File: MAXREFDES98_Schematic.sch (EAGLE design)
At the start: 17 parts, among them T1 TG110-S055N2RL

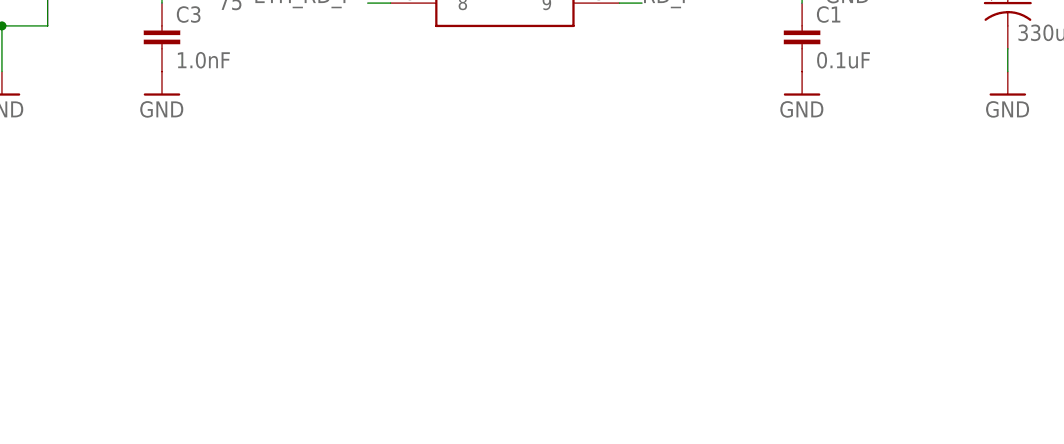
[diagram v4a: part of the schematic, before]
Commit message: Added ethernet jumpers
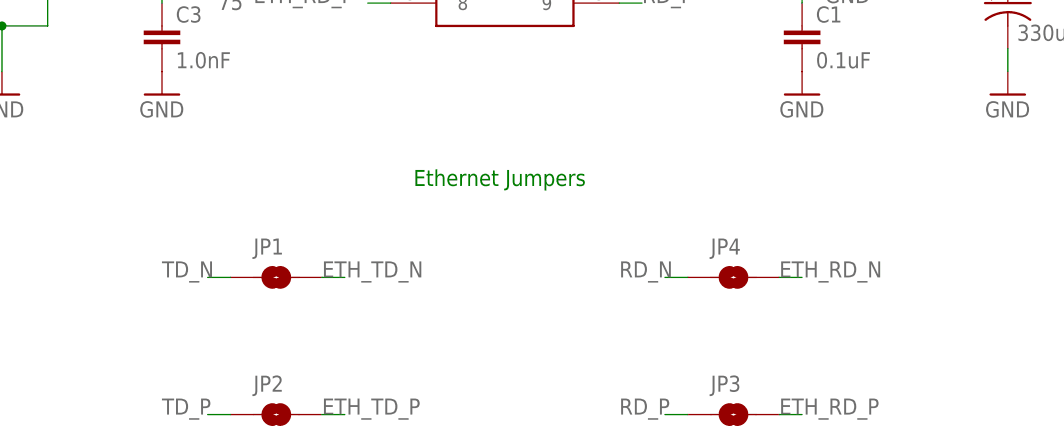
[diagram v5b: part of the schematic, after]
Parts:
- added JP1, JP2, JP3, JP4: JUMPER-SMT_2_NO_NO-SILK, SparkFun-Jumpers:JUMPER-SMT_2_NO_NO-SILK
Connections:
- net ETH_RD_N: now also JP4.2
- net ETH_RD_P: now also JP3.2
- net ETH_TD_N: now also JP1.2
- net ETH_TD_P: now also JP2.2
- net RD_N: now also JP4.1
- net RD_P: now also JP3.1
- net TD_N: now also JP1.1
- net TD_P: now also JP2.1
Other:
- note added: "Ethernet Jumpers"
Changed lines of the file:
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@@
 <part name="GND8" library="supply1" library_urn="urn:adsk.eagle:library:371" deviceset="GND" device=""/>
 <part name="R6" library="SparkFun-Resistors" library_urn="urn:adsk.eagle:library:532" deviceset="0OHM" device="-0603-1/10W-5%" package3d_urn="urn:adsk.eagle:package:39650/1" value="470"/>
+<part name="JP1" library="SparkFun-Jumpers" library_urn="urn:adsk.eagle:library:528" deviceset="JUMPER-SMT_2_NO" device="_NO-SILK" package3d_urn="urn:adsk.eagle:package:39277/1"/>
+<part name="JP2" library="SparkFun-Jumpers" library_urn="urn:adsk.eagle:library:528" deviceset="JUMPER-SMT_2_NO" device="_NO-SILK" package3d_urn="urn:adsk.eagle:package:39277/1"/>
+<part name="JP3" library="SparkFun-Jumpers" library_urn="urn:adsk.eagle:library:528" deviceset="JUMPER-SMT_2_NO" device="_NO-SILK" package3d_urn="urn:adsk.eagle:package:39277/1"/>
+<part name="JP4" library="SparkFun-Jumpers" library_urn="urn:adsk.eagle:library:528" deviceset="JUMPER-SMT_2_NO" device="_NO-SILK" package3d_urn="urn:adsk.eagle:package:39277/1"/>
 </parts>
 <sheets>
@@
 <text x="180.34" y="76.2" size="1.778" layer="91">Indicator LEDs</text>
 <text x="236.22" y="86.36" size="1.778" layer="91">Nano Pi</text>
+<text x="96.52" y="33.02" size="1.778" layer="91">Ethernet Jumpers</text>
 </plain>
 <instances>
@@
 <attribute name="NAME" x="176.276" y="60.96" size="1.778" layer="95" font="vector" rot="R90" align="bottom-center"/>
 <attribute name="VALUE" x="179.324" y="60.96" size="1.778" layer="96" font="vector" rot="R90" align="top-center"/>
+</instance>
+<instance part="JP1" gate="G$1" x="81.28" y="22.86" smashed="yes">
+<attribute name="NAME" x="78.74" y="25.4" size="1.778" layer="95" font="vector"/>
+</instance>
+<instance part="JP2" gate="G$1" x="81.28" y="7.62" smashed="yes">
+<attribute name="NAME" x="78.74" y="10.16" size="1.778" layer="95" font="vector"/>
+</instance>
+<instance part="JP3" gate="G$1" x="132.08" y="7.62" smashed="yes">
+<attribute name="NAME" x="129.54" y="10.16" size="1.778" layer="95" font="vector"/>
+</instance>
+<instance part="JP4" gate="G$1" x="132.08" y="22.86" smashed="yes">
+<attribute name="NAME" x="129.54" y="25.4" size="1.778" layer="95" font="vector"/>
 </instance>
 </instances>
@@
 <label x="25.4" y="58.42" size="1.778" layer="95"/>
 </segment>
+<segment>
+<pinref part="JP4" gate="G$1" pin="1"/>
+<wire x1="127" y1="22.86" x2="124.46" y2="22.86" width="0.1524" layer="91"/>
+<label x="119.38" y="22.86" size="1.778" layer="95"/>
+</segment>
 </net>
 <net name="RD_P" class="1">
@@
 <label x="25.4" y="60.96" size="1.778" layer="95"/>
 </segment>
+<segment>
+<pinref part="JP3" gate="G$1" pin="1"/>
+<wire x1="127" y1="7.62" x2="124.46" y2="7.62" width="0.1524" layer="91"/>
+<label x="119.38" y="7.62" size="1.778" layer="95"/>
+</segment>
 </net>
 <net name="TD_N" class="1">
@@
 <label x="25.4" y="53.34" size="1.778" layer="95"/>
 </segment>
+<segment>
+<pinref part="JP1" gate="G$1" pin="1"/>
+<wire x1="76.2" y1="22.86" x2="73.66" y2="22.86" width="0.1524" layer="91"/>
+<label x="68.58" y="22.86" size="1.778" layer="95"/>
+</segment>
 </net>
 <net name="TD_P" class="1">
@@
 <wire x1="22.86" y1="55.88" x2="25.4" y2="55.88" width="0.1524" layer="91"/>
 <label x="25.4" y="55.88" size="1.778" layer="95"/>
+</segment>
+<segment>
+<pinref part="JP2" gate="G$1" pin="1"/>
+<wire x1="76.2" y1="7.62" x2="73.66" y2="7.62" width="0.1524" layer="91"/>
+<label x="68.58" y="7.62" size="1.778" layer="95"/>
 </segment>
 </net>
@@
 <pinref part="U$2" gate="G$1" pin="TD-"/>
 </segment>
+<segment>
+<pinref part="JP1" gate="G$1" pin="2"/>
+<wire x1="86.36" y1="22.86" x2="88.9" y2="22.86" width="0.1524" layer="91"/>
+<label x="86.36" y="22.86" size="1.778" layer="95"/>
+</segment>
 </net>
 <net name="N$11" class="0">
@@
 <pinref part="U$2" gate="G$1" pin="TD+"/>
 </segment>
+<segment>
+<pinref part="JP2" gate="G$1" pin="2"/>
+<wire x1="86.36" y1="7.62" x2="88.9" y2="7.62" width="0.1524" layer="91"/>
+<label x="86.36" y="7.62" size="1.778" layer="95"/>
+</segment>
 </net>
 <net name="ETH_RD_N" class="0">
@@
 <pinref part="U$2" gate="G$1" pin="RD-"/>
 </segment>
+<segment>
+<pinref part="JP4" gate="G$1" pin="2"/>
+<wire x1="137.16" y1="22.86" x2="139.7" y2="22.86" width="0.1524" layer="91"/>
+<label x="137.16" y="22.86" size="1.778" layer="95"/>
+</segment>
 </net>
 <net name="ETH_RD_P" class="0">
@@
 <pinref part="U$2" gate="G$1" pin="RD+"/>
 </segment>
-</net>
+<segment>
+<pinref part="JP3" gate="G$1" pin="2"/>
+<wire x1="137.16" y1="7.62" x2="139.7" y2="7.62" width="0.1524" layer="91"/>
+<label x="137.16" y="7.62" size="1.778" layer="95"/>
+</segment>
+</net>
